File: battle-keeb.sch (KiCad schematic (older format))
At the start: 61 parts, among them J1 Conn_01x06_Male, J2 USB_C_Receptacle_USB2.0, SW1 SW_Push, SW2 Rotary_Encoder_Switch, SW3 Rotary_Encoder_Switch, SW4 Rotary_Encoder_Switch, U1 ATmega32U4-AU, Y1 16MHz

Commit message: Layout Start
Layout started. USB-C Footprint needs work.
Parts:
- J2: footprint Type-C:HRO-TYPE-C-31-M-12-HandSoldering -> Type-C:HRO-TYPE-C-31-M-12
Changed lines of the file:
@@
 F 0 "J2" H 9707 3167 50  0000 C CNN
 F 1 "USB_C_Receptacle_USB2.0" H 9707 3076 50  0000 C CNN
-F 2 "Type-C:HRO-TYPE-C-31-M-12-HandSoldering" H 9750 2300 50  0001 C CNN
+F 2 "Type-C:HRO-TYPE-C-31-M-12" H 9750 2300 50  0001 C CNN
 F 3 "https://www.usb.org/sites/default/files/documents/usb_type-c.zip" H 9750 2300 50  0001 C CNN
 	1    9600 2300

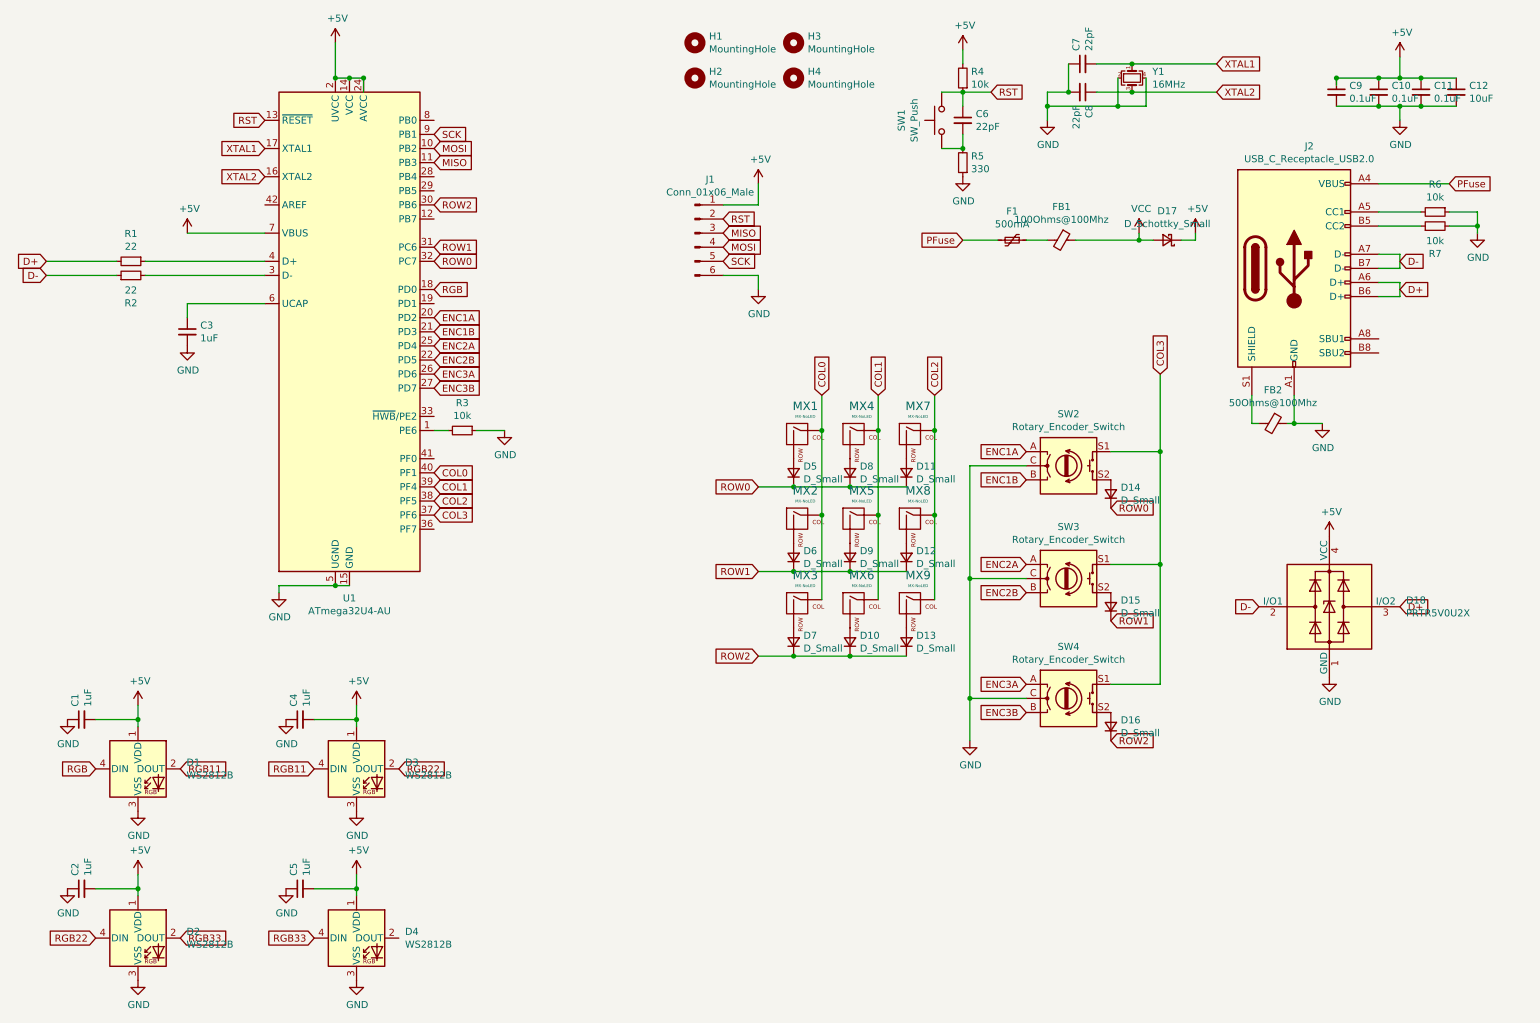
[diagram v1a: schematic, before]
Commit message: Placement and Schematic Update
Fixed USB-C Connector on schematic and layout - wurth connector for hand assembly. Placed and adjusted components for control, EMI/EMC, USB, JTAG, and other components.
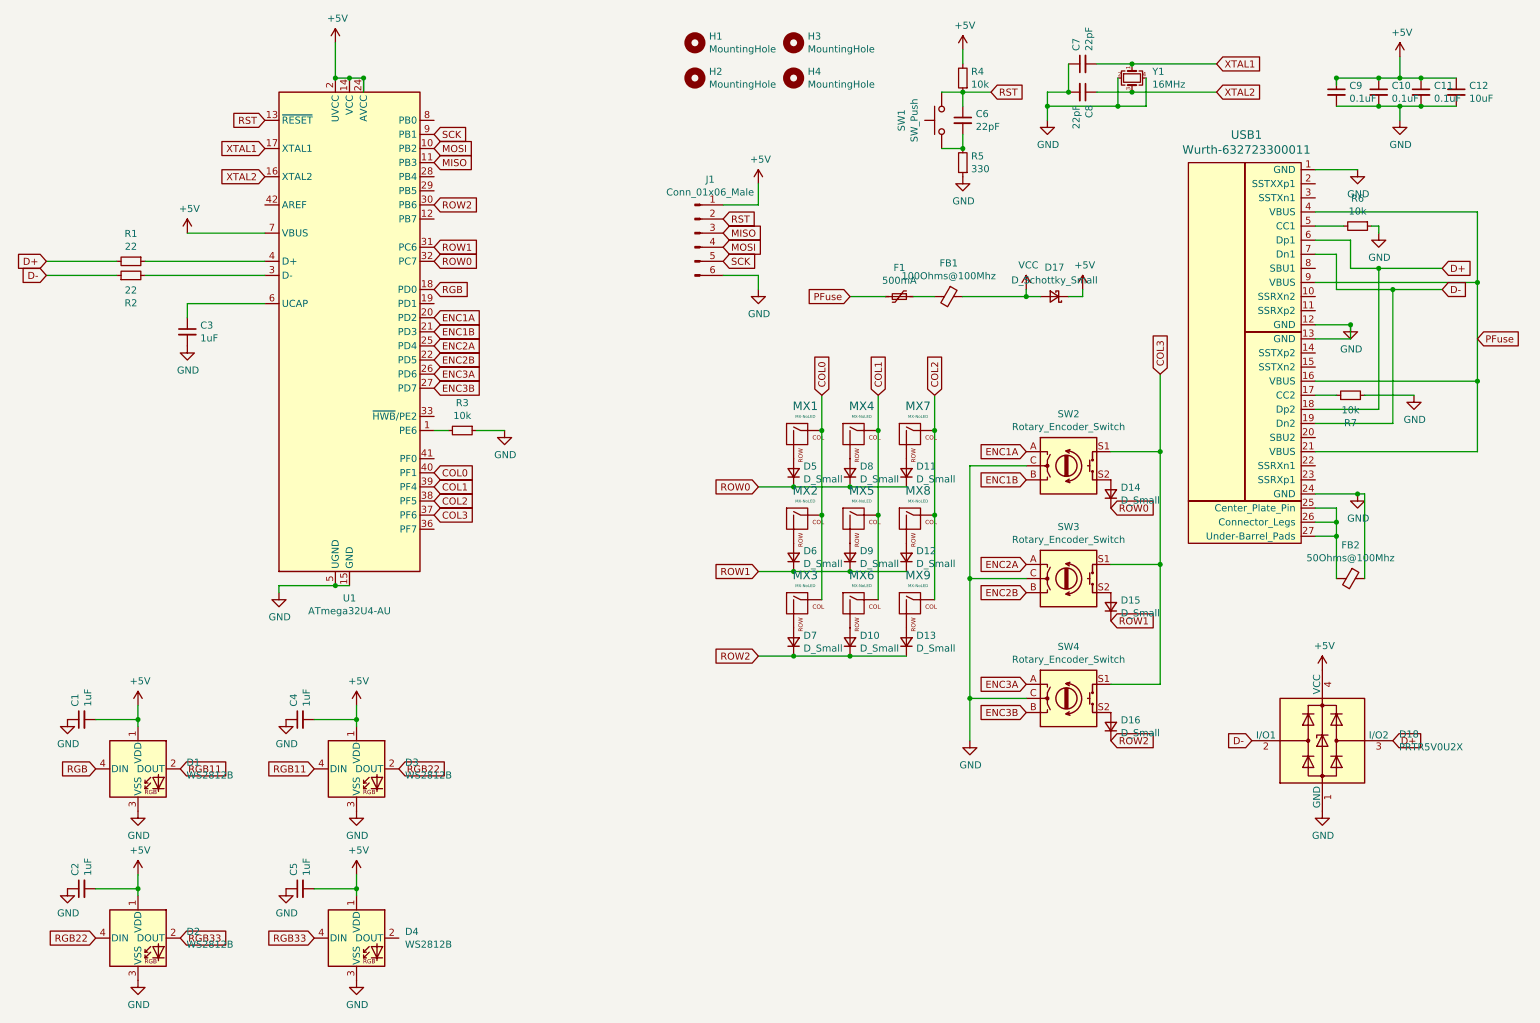
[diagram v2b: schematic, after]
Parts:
- removed J2: USB_C_Receptacle_USB2.0, Type-C:HRO-TYPE-C-31-M-12, symbol Connector:USB_C_Receptacle_USB2.0
- added USB1: Wurth-632723300011, Type-C:Wurth-632723300011-HandSoldering, symbol Type-C:Wurth-632723300011
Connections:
- net D+: now also USB1.18 (Dp2), USB1.6 (Dp1)
- net D-: now also USB1.19 (Dn2), USB1.7 (Dn1)
- net GND: now also USB1.1 (GND), USB1.12 (GND), USB1.13 (GND), USB1.24 (GND)
- net PFuse: now also USB1.16 (VBUS), USB1.21 (VBUS), USB1.4 (VBUS), USB1.9 (VBUS)
- net at R6.2: now also USB1.5 (CC1)
- net at R7.1: now also USB1.17 (CC2)
- net at FB2.2: now also USB1.25 (Center_Plate_Pin), USB1.26 (Connector_Legs), USB1.27 (Under-Barrel_Pads)
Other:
- moved on the sheet: D17, D18, F1, FB1, FB2, R6, R7
